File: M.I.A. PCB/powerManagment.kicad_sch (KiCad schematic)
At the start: 41 parts, among them J14 Screw_Terminal_01x02, J18 Screw_Terminal_01x02, J2 Conn_01x02_Pin, U10 AP2112K-3.3, U11 INA219AxDCN, U12 AP62150WU, U13 TPS2121RUXR, U14 AP62150WU, U9 TPS2121RUXR

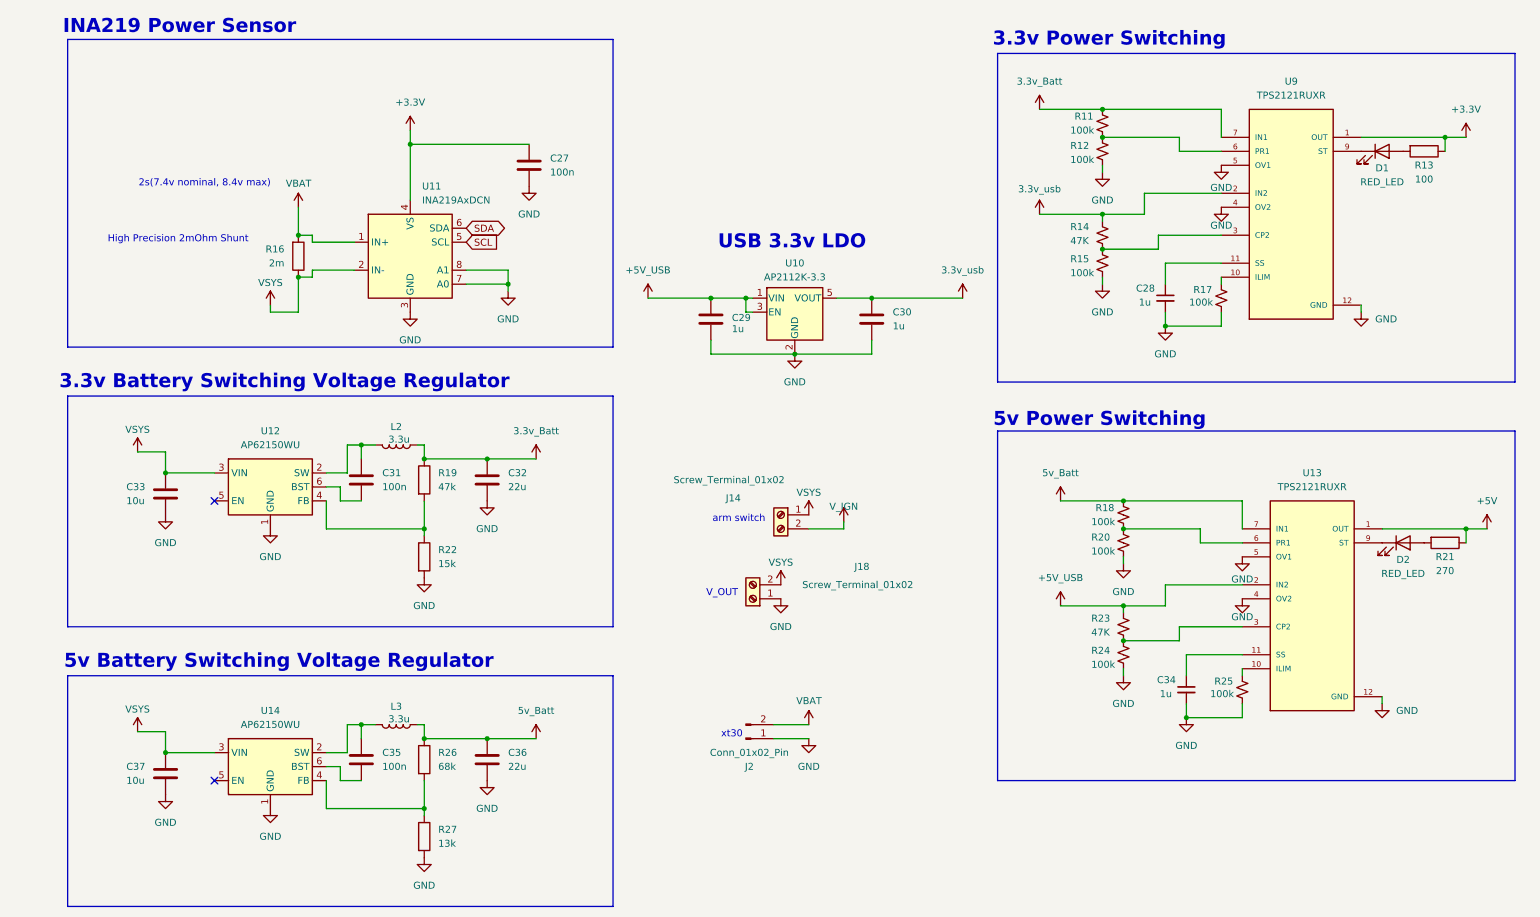
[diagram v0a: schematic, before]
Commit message: Updated top connectors to be TLM_SPI
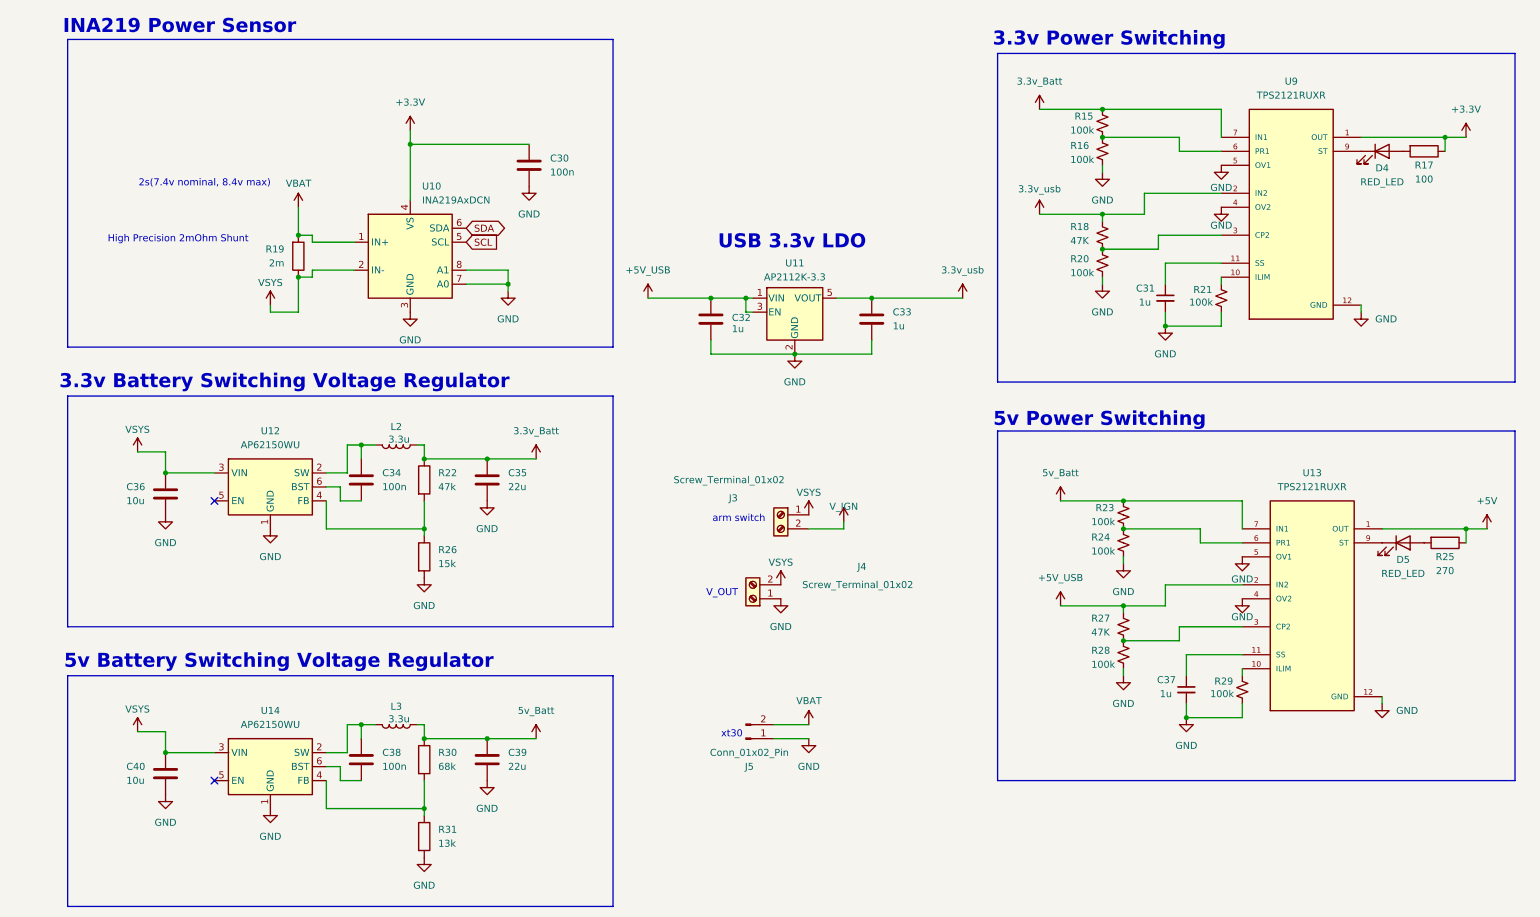
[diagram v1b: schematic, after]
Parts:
- renumbered C27 to C30, C28 to C31, C29 to C32, C30 to C33, C31 to C34, C32 to C35, C33 to C36, C34 to C37, C35 to C38, C36 to C39, C37 to C40, D1 to D4, D2 to D5, J14 to J3, J18 to J4, J2 to J5, R11 to R15, R12 to R16, R13 to R17, R14 to R18, R16 to R19, R15 to R20, R17 to R21, R19 to R22, R18 to R23, R20 to R24, R21 to R25, R22 to R26, R23 to R27, R24 to R28, R25 to R29, R26 to R30, R27 to R31, U11 to U10, U10 to U11

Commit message: More Small Updates/Improvements
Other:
- note added: "Power Connectors"
- note added: "XT30 Input"
- note removed: "xt30"
- moved on the sheet: C31, C32, C33, C37, D4, D5, J3, J5, R15, R16, R17, R18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
